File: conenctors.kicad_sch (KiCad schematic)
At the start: 4 parts, among them J1 Conn_01x04_Pin, J2 Conn_01x04_Pin, J3 Conn_01x09, J4 Conn_02x03_Odd_Even

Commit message: assign footprints
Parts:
- J1, J2: footprint (none) -> Connector_PinHeader_2.54mm:PinHeader_1x04_P2.54mm_Vertical
- J3: footprint (none) -> Connector_PinHeader_2.54mm:PinHeader_1x09_P2.54mm_Vertical
- J4: footprint (none) -> Connector_PinHeader_2.54mm:PinHeader_2x03_P2.54mm_Vertical
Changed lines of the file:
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@@
 			)
 		)
-		(property "Footprint" ""
+		(property "Footprint" "Connector_PinHeader_2.54mm:PinHeader_2x03_P2.54mm_Vertical"
 			(at 223.52 68.58 0)
 			(effects
@@
 			)
 		)
-		(property "Footprint" ""
+		(property "Footprint" "Connector_PinHeader_2.54mm:PinHeader_1x04_P2.54mm_Vertical"
 			(at 146.05 67.31 0)
 			(effects
@@
 			)
 		)
-		(property "Footprint" ""
+		(property "Footprint" "Connector_PinHeader_2.54mm:PinHeader_1x04_P2.54mm_Vertical"
 			(at 167.64 67.31 0)
 			(effects
@@
 			)
 		)
-		(property "Footprint" ""
+		(property "Footprint" "Connector_PinHeader_2.54mm:PinHeader_1x09_P2.54mm_Vertical"
 			(at 196.85 60.96 0)
 			(effects

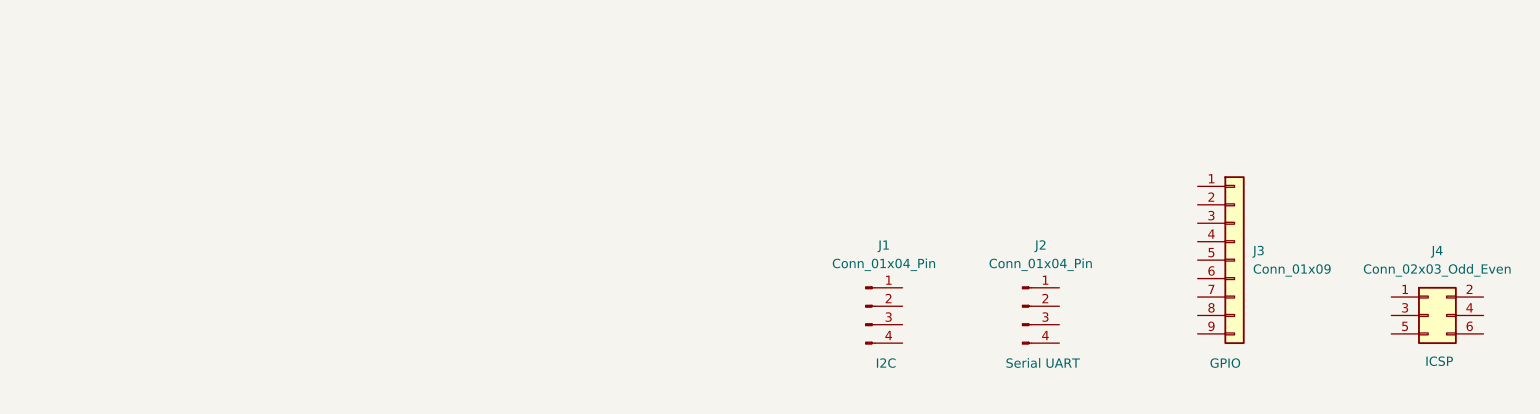
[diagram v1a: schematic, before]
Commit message: complete wiring and perform ERC
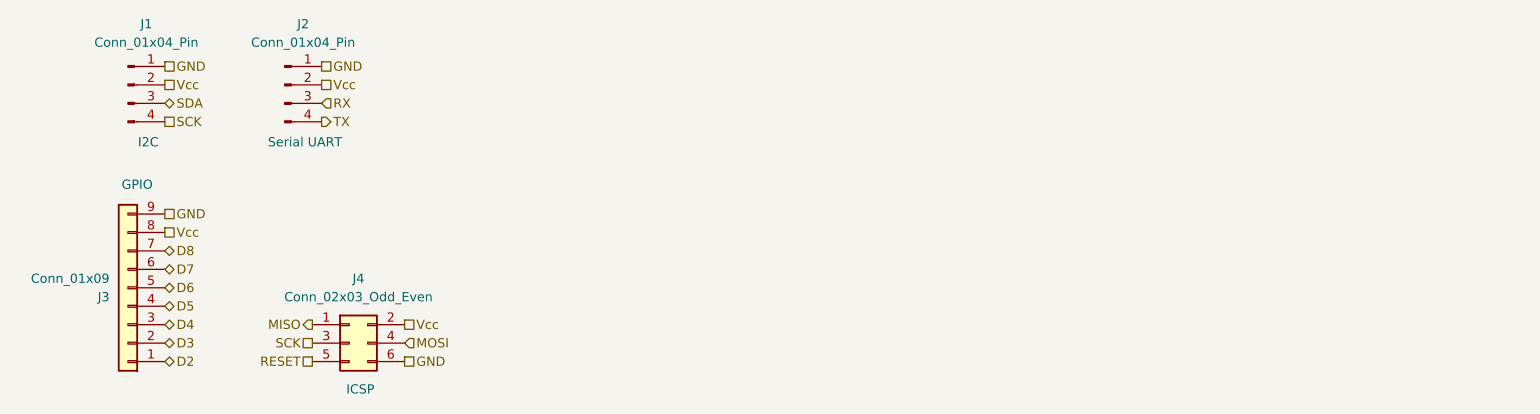
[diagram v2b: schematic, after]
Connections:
- net MISO: now reaches J4.1 (Pin_1)
- net Vcc: now reaches J4.2 (Pin_2)
- net Vcc: now also J1.2 (Pin_2), J2.2 (Pin_2), J3.8 (Pin_8)
- net SCK: now reaches J4.3 (Pin_3)
- net SCK: now also J1.4 (Pin_4)
- net MOSI: now reaches J4.4 (Pin_4)
- net RESET: now reaches J4.5 (Pin_5)
- net GND: now reaches J4.6 (Pin_6)
- net GND: now also J1.1 (Pin_1), J2.1 (Pin_1), J3.9 (Pin_9)
- net SDA: now reaches J1.3 (Pin_3)
- net RX: now reaches J2.3 (Pin_3)
- net TX: now reaches J2.4 (Pin_4)
- net D2: now reaches J3.1 (Pin_1)
- net D3: now reaches J3.2 (Pin_2)
- net D4: now reaches J3.3 (Pin_3)
- net D5: now reaches J3.4 (Pin_4)
- net D6: now reaches J3.5 (Pin_5)
- net D7: now reaches J3.6 (Pin_6)
- net D8: now reaches J3.7 (Pin_7)
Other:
- moved on the sheet: J1, J2, J3, J4

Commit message: fix some routes and add copper fills
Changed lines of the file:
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@@
 		)
 		(property "Purpose" "GPIO"
-			(at 45.72 50.546 0)
+			(at 45.212 78.74 0)
 			(effects
 				(font

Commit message: fix bug in the schematic with SCK and SCL wires
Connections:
- net SCK: no longer J1.4 (Pin_4)
- new net SCL: J1.4 (Pin_4)
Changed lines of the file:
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@@
 		)
 	)
-	(hierarchical_label "SCK"
+	(hierarchical_label "SCL"
 		(shape passive)
 		(at 49.53 41.91 0)
